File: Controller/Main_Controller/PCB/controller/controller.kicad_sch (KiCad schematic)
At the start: 253 parts, among them J1 Conn_01x10, M1 Motor_DC, Q1 S9013, Q10 S9013, Q11 S9013, Q12 S9013, Q13 S9013, Q14 S9013, Q15 S9013, Q16 S9013, Q17 S9013, Q18 S9013, Q19 S9013, Q2 S9013, Q20 S9013, Q21 S9013, Q22 S9013, Q23 S9013, Q24 S9013, Q25 Q_PMOS_DGS, Q26 Q_NMOS_DGS, Q27 S9013, Q3 S9013, Q4 S9013, Q5 S9013, Q6 S9013, Q7 S9013, Q8 S9013, Q9 S9013, SW1 SW_SPDT, SW2 SW_SPDT, U1 NUCLEO-L432KC, U10 ZLDO1117G50TA, U2 NUCLEO144-F429ZI, U3 74HC14, U4 74HC14, U5 74HC14, U6 Joystick, U7 Joystick, U8 HY1602E, U9 ZSR330GTA

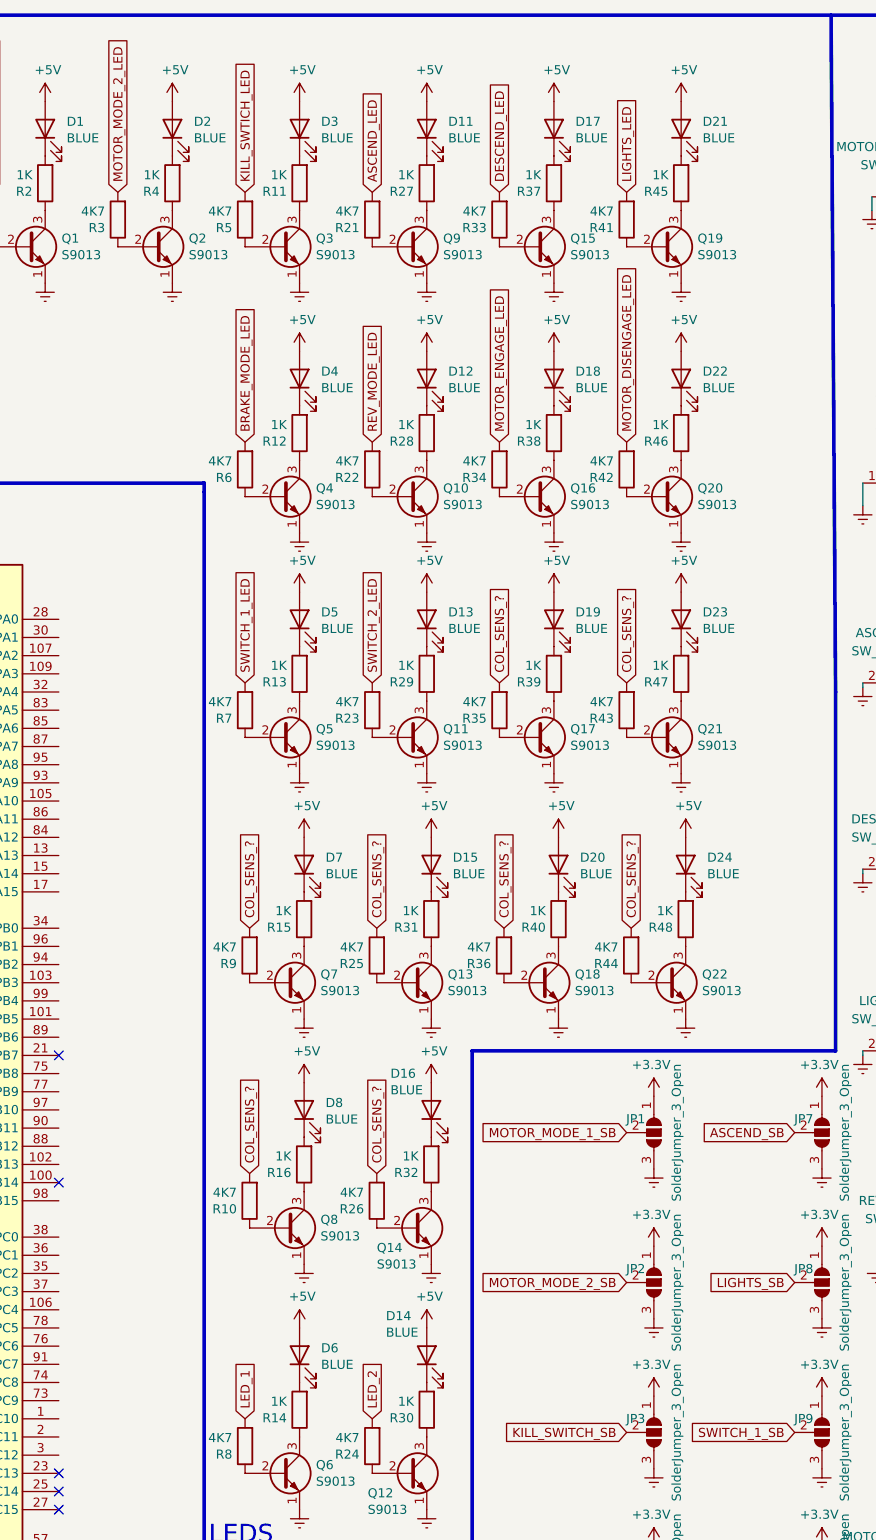
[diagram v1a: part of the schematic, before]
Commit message: LED colours and resistor values
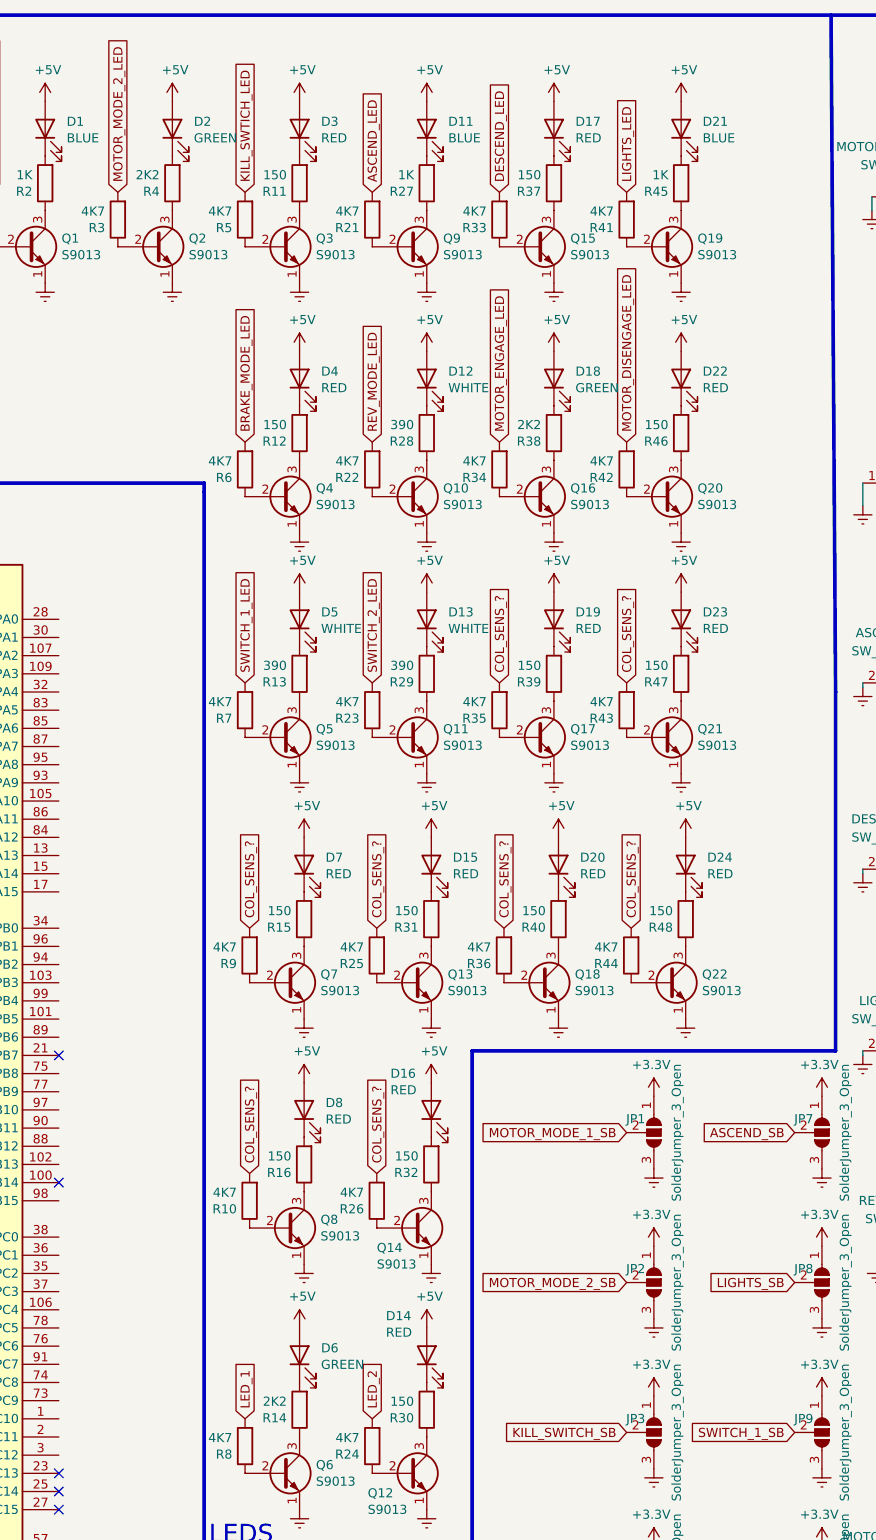
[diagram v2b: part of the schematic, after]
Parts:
- D12, D13, D5: value BLUE -> WHITE
- D14, D15, D16, D17, D19, D20, D22, D23, D24, D3, D4, D7, D8: value BLUE -> RED
- D18, D2, D6: value BLUE -> GREEN
- R11, R12, R15, R16, R30, R31, R32, R37, R39, R40, R46, R47, R48: value 1K -> 150
- R13, R28, R29: value 1K -> 390
- R14, R38, R4: value 1K -> 2K2
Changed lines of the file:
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@@
       (effects (font (size 1.27 1.27)) (justify left))
     )
-    (property "Value" "1K" (at 120.777 171.577 0)
+    (property "Value" "150" (at 120.777 171.577 0)
       (effects (font (size 1.27 1.27)) (justify left))
     )
@@
       (effects (font (size 1.27 1.27)) (justify right))
     )
-    (property "Value" "BLUE" (at 178.8922 132.1308 90)
+    (property "Value" "RED" (at 178.8922 132.1308 90)
       (effects (font (size 1.27 1.27)) (justify right))
     )
@@
       (effects (font (size 1.27 1.27)) (justify right))
     )
-    (property "Value" "BLUE" (at 107.1372 29.2608 90)
+    (property "Value" "GREEN" (at 107.1372 29.2608 90)
       (effects (font (size 1.27 1.27)) (justify right))
     )
@@
       (effects (font (size 1.27 1.27)) (justify right))
     )
-    (property "Value" "BLUE" (at 134.62 162.3314 90)
+    (property "Value" "RED" (at 134.62 162.3314 90)
       (effects (font (size 1.27 1.27)) (justify right))
     )
@@
       (effects (font (size 1.27 1.27)) (justify right))
     )
-    (property "Value" "BLUE" (at 160.4772 64.1858 90)
+    (property "Value" "GREEN" (at 160.4772 64.1858 90)
       (effects (font (size 1.27 1.27)) (justify right))
     )
@@
       (effects (font (size 1.27 1.27)) (justify left))
     )
-    (property "Value" "1K" (at 137.922 102.997 0)
+    (property "Value" "390" (at 137.922 102.997 0)
       (effects (font (size 1.27 1.27)) (justify left))
     )
@@
       (effects (font (size 1.27 1.27)) (justify left))
     )
-    (property "Value" "1K" (at 174.117 137.287 0)
+    (property "Value" "150" (at 174.117 137.287 0)
       (effects (font (size 1.27 1.27)) (justify left))
     )
@@
       (effects (font (size 1.27 1.27)) (justify right))
     )
-    (property "Value" "BLUE" (at 160.4772 97.8408 90)
+    (property "Value" "RED" (at 160.4772 97.8408 90)
       (effects (font (size 1.27 1.27)) (justify right))
     )
@@
       (effects (font (size 1.27 1.27)) (justify left))
     )
-    (property "Value" "1K" (at 120.142 205.867 0)
+    (property "Value" "2K2" (at 120.142 205.867 0)
       (effects (font (size 1.27 1.27)) (justify left))
     )
@@
       (effects (font (size 1.27 1.27)) (justify left))
     )
-    (property "Value" "1K" (at 155.702 69.342 0)
+    (property "Value" "2K2" (at 155.702 69.342 0)
       (effects (font (size 1.27 1.27)) (justify left))
     )
@@
       (effects (font (size 1.27 1.27)) (justify left))
     )
-    (property "Value" "1K" (at 102.362 34.417 0)
+    (property "Value" "2K2" (at 102.362 34.417 0)
       (effects (font (size 1.27 1.27)) (justify left))
     )
@@
       (effects (font (size 1.27 1.27)) (justify left))
     )
-    (property "Value" "1K" (at 138.557 171.577 0)
+    (property "Value" "150" (at 138.557 171.577 0)
       (effects (font (size 1.27 1.27)) (justify left))
     )
@@
       (effects (font (size 1.27 1.27)) (justify right))
     )
-    (property "Value" "BLUE" (at 124.9172 97.8408 90)
+    (property "Value" "WHITE" (at 124.9172 97.8408 90)
       (effects (font (size 1.27 1.27)) (justify right))
     )
@@
       (effects (font (size 1.27 1.27)) (justify left))
     )
-    (property "Value" "1K" (at 156.337 137.287 0)
+    (property "Value" "150" (at 156.337 137.287 0)
       (effects (font (size 1.27 1.27)) (justify left))
     )
@@
       (effects (font (size 1.27 1.27)) (justify right))
     )
-    (property "Value" "BLUE" (at 178.2572 97.8408 90)
+    (property "Value" "RED" (at 178.2572 97.8408 90)
       (effects (font (size 1.27 1.27)) (justify right))
     )
@@
       (effects (font (size 1.27 1.27)) (justify right))
     )
-    (property "Value" "BLUE" (at 124.9172 29.2608 90)
+    (property "Value" "RED" (at 124.9172 29.2608 90)
       (effects (font (size 1.27 1.27)) (justify right))
     )
@@
       (effects (font (size 1.27 1.27)) (justify right))
     )
-    (property "Value" "BLUE" (at 142.6972 97.8408 90)
+    (property "Value" "WHITE" (at 142.6972 97.8408 90)
       (effects (font (size 1.27 1.27)) (justify right))
     )
@@
       (effects (font (size 1.27 1.27)) (justify right))
     )
-    (property "Value" "BLUE" (at 133.985 196.215 90)
+    (property "Value" "RED" (at 133.985 196.215 90)
       (effects (font (size 1.27 1.27)) (justify right))
     )
@@
       (effects (font (size 1.27 1.27)) (justify right))
     )
-    (property "Value" "BLUE" (at 142.6972 64.1858 90)
+    (property "Value" "WHITE" (at 142.6972 64.1858 90)
       (effects (font (size 1.27 1.27)) (justify right))
     )
@@
       (effects (font (size 1.27 1.27)) (justify left))
     )
-    (property "Value" "1K" (at 155.702 102.997 0)
+    (property "Value" "150" (at 155.702 102.997 0)
       (effects (font (size 1.27 1.27)) (justify left))
     )
@@
       (effects (font (size 1.27 1.27)) (justify right))
     )
-    (property "Value" "BLUE" (at 124.9172 200.7108 90)
+    (property "Value" "GREEN" (at 124.9172 200.7108 90)
       (effects (font (size 1.27 1.27)) (justify right))
     )
@@
       (effects (font (size 1.27 1.27)) (justify right))
     )
-    (property "Value" "BLUE" (at 125.5522 132.1308 90)
+    (property "Value" "RED" (at 125.5522 132.1308 90)
       (effects (font (size 1.27 1.27)) (justify right))
     )
@@
       (effects (font (size 1.27 1.27)) (justify left))
     )
-    (property "Value" "1K" (at 138.557 137.287 0)
+    (property "Value" "150" (at 138.557 137.287 0)
       (effects (font (size 1.27 1.27)) (justify left))
     )
@@
       (effects (font (size 1.27 1.27)) (justify right))
     )
-    (property "Value" "BLUE" (at 125.5522 166.4208 90)
+    (property "Value" "RED" (at 125.5522 166.4208 90)
       (effects (font (size 1.27 1.27)) (justify right))
     )
@@
       (effects (font (size 1.27 1.27)) (justify right))
     )
-    (property "Value" "BLUE" (at 161.1122 132.1308 90)
+    (property "Value" "RED" (at 161.1122 132.1308 90)
       (effects (font (size 1.27 1.27)) (justify right))
     )
@@
       (effects (font (size 1.27 1.27)) (justify left))
     )
-    (property "Value" "1K" (at 155.702 34.417 0)
+    (property "Value" "150" (at 155.702 34.417 0)
       (effects (font (size 1.27 1.27)) (justify left))
     )
@@
       (effects (font (size 1.27 1.27)) (justify left))
     )
-    (property "Value" "1K" (at 120.142 34.417 0)
+    (property "Value" "150" (at 120.142 34.417 0)
       (effects (font (size 1.27 1.27)) (justify left))
     )
@@
       (effects (font (size 1.27 1.27)) (justify right))
     )
-    (property "Value" "BLUE" (at 143.3322 132.1308 90)
+    (property "Value" "RED" (at 143.3322 132.1308 90)
       (effects (font (size 1.27 1.27)) (justify right))
     )
@@
       (effects (font (size 1.27 1.27)) (justify left))
     )
-    (property "Value" "1K" (at 137.922 205.867 0)
+    (property "Value" "150" (at 137.922 205.867 0)
       (effects (font (size 1.27 1.27)) (justify left))
     )
@@
       (effects (font (size 1.27 1.27)) (justify left))
     )
-    (property "Value" "1K" (at 120.142 102.997 0)
+    (property "Value" "390" (at 120.142 102.997 0)
       (effects (font (size 1.27 1.27)) (justify left))
     )
@@
       (effects (font (size 1.27 1.27)) (justify left))
     )
-    (property "Value" "1K" (at 120.777 137.287 0)
+    (property "Value" "150" (at 120.777 137.287 0)
       (effects (font (size 1.27 1.27)) (justify left))
     )
@@
       (effects (font (size 1.27 1.27)) (justify right))
     )
-    (property "Value" "BLUE" (at 124.9172 64.1858 90)
+    (property "Value" "RED" (at 124.9172 64.1858 90)
       (effects (font (size 1.27 1.27)) (justify right))
     )
@@
       (effects (font (size 1.27 1.27)) (justify left))
     )
-    (property "Value" "1K" (at 173.482 102.997 0)
+    (property "Value" "150" (at 173.482 102.997 0)
       (effects (font (size 1.27 1.27)) (justify left))
     )
@@
       (effects (font (size 1.27 1.27)) (justify right))
     )
-    (property "Value" "BLUE" (at 160.4772 29.2608 90)
+    (property "Value" "RED" (at 160.4772 29.2608 90)
       (effects (font (size 1.27 1.27)) (justify right))
     )
@@
       (effects (font (size 1.27 1.27)) (justify left))
     )
-    (property "Value" "1K" (at 173.482 69.342 0)
+    (property "Value" "150" (at 173.482 69.342 0)
       (effects (font (size 1.27 1.27)) (justify left))
     )
@@
       (effects (font (size 1.27 1.27)) (justify left))
     )
-    (property "Value" "1K" (at 137.922 69.342 0)
+    (property "Value" "390" (at 137.922 69.342 0)
       (effects (font (size 1.27 1.27)) (justify left))
     )
@@
       (effects (font (size 1.27 1.27)) (justify right))
     )
-    (property "Value" "BLUE" (at 178.2572 64.1858 90)
+    (property "Value" "RED" (at 178.2572 64.1858 90)
       (effects (font (size 1.27 1.27)) (justify right))
     )
@@
       (effects (font (size 1.27 1.27)) (justify left))
     )
-    (property "Value" "1K" (at 120.142 69.342 0)
+    (property "Value" "150" (at 120.142 69.342 0)
       (effects (font (size 1.27 1.27)) (justify left))
     )
